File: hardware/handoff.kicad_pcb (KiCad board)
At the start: 2 copper layers, 40 x 62 mm, 55 parts, among them J1 BAT XH-2, J2 PAD JST-XH 2p, J3 LED JST-XH 4p / 5mm RGB, J5 CHG XH-2, J6 MOT 1x02 2.54, Q1 AO3400A, SW1 SS-12F23G5, SW2 TACT 6x6, U1 Raspberry Pi Pico 2 W, U2 MCP6292-E/MS

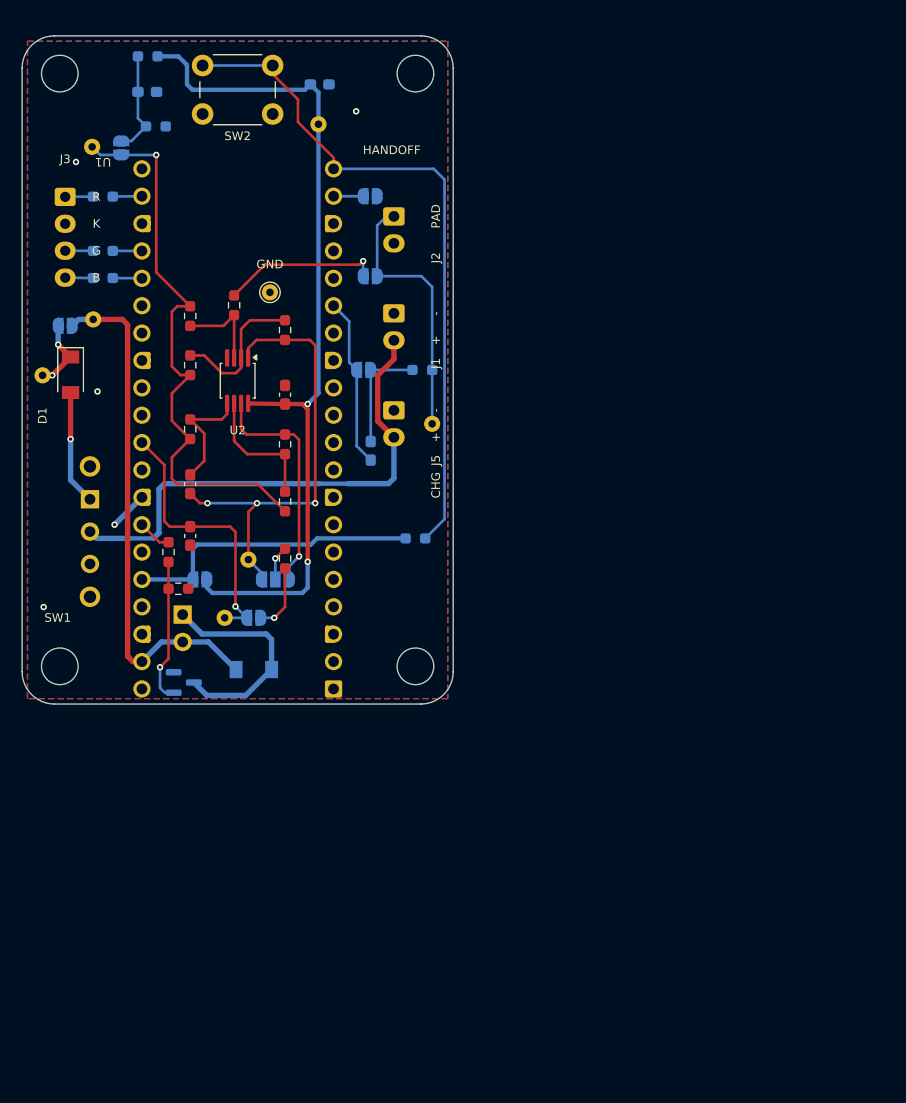
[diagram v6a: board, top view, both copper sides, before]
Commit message: Put the board on the sheet, with fab notes beside it and a title block
The board sat on the page origin, over the sheet border, with a one-line
fab note written across the copper. It now sits at PAGE (40, 35) on the A4
sheet: vec() adds the offset going into pcbnew and at() takes it off coming
out, so every coordinate in gen_pcb.py stays in the floor plan's frame. The
zone outlines appended raw mm() values instead of vec() and are fixed. The
aux and grid origins are the board corner and the fab pack is plotted from
it, so Gerber and drill coordinates are unchanged by the move.

The fab note is a numbered FABRICATION NOTES block on Cmts.User to the
right of the board, and the title block is filled from a SHEET constant
shared with gen_schematic.py so the board and the sheet cannot disagree.

Moving the board exposed a real bug: a fresh BOARD() has no connectivity
until BuildConnectivity() is called, and ZONE_FILLER's island test read
that uninitialised state - the bottom pour's little-finger-wall strip was
kept or dropped, or the whole pour came out empty, depending on where the
board sat. Connectivity is now built before the fill.

Also carries the routing tidy that was in the working tree: AGND's tie out
of pin 33 straight west; TP7 east of D1 on the cathode row with no via;
BTN leaving pin 20 at 45 straight out of the pad; R15 under the Pico on
the +3V3 branch's own row. DRC 0 errors, parity 0, unrouted 0, shorts 0,
19 vias, fab pack 17 files.

Co-Authored-By: Claude Opus 5 <noreply@anthropic.com>
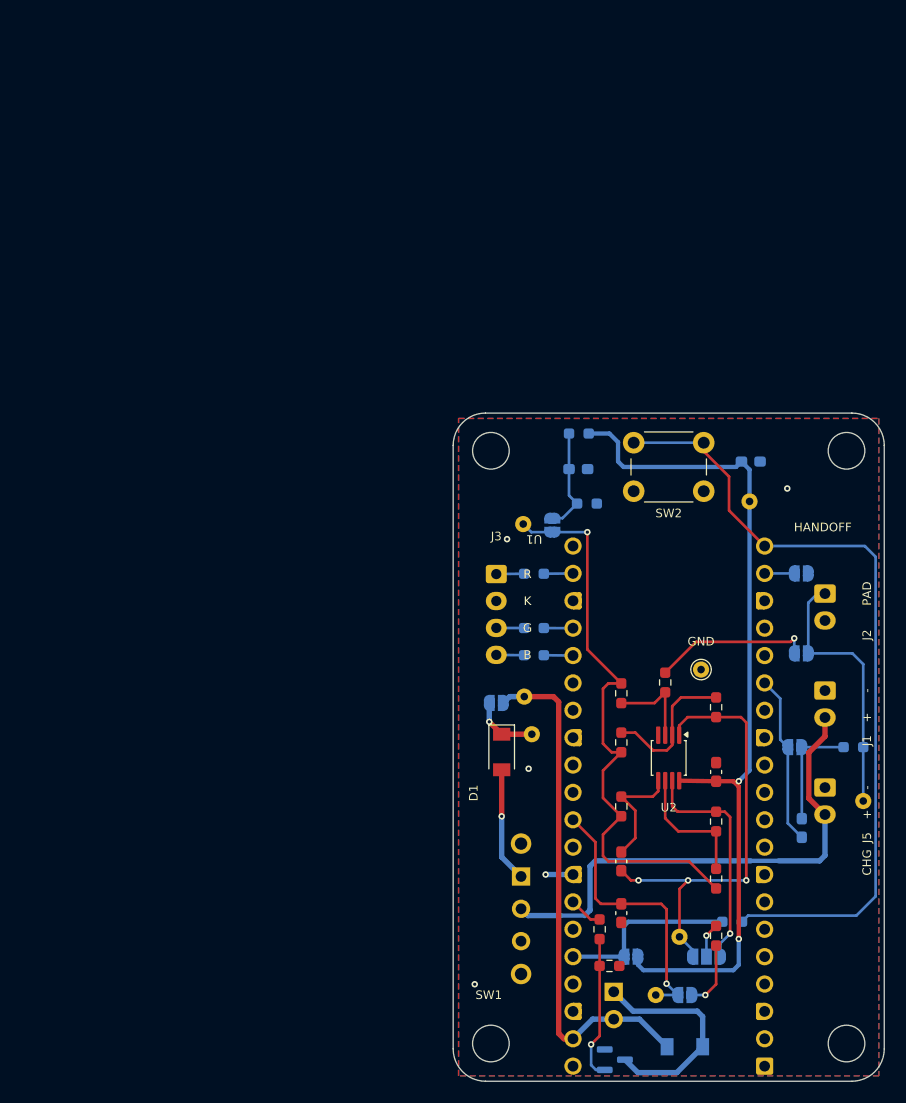
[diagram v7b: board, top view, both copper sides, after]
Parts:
- moved TP7 56.3 mm to (47.3, 64.8)
- moved JP7 53.2 mm to (72.3, 57.3)
- moved JP8 53.2 mm to (72.3, 49.9)
- moved TP8 53.2 mm to (67.5, 43.2)
- moved C2 53.2 mm to (55.6, 81.4)
- moved R7 53.2 mm to (64.4, 72.9)
- moved C3 53.2 mm to (64.4, 68.3)
- moved C4 53.2 mm to (51.6, 40.2)
- moved C5 53.2 mm to (67.6, 39.5)
- moved D1 53.2 mm to (44.5, 66.5)
- moved D3 53.2 mm to (61.5, 93.8)
- moved H1 53.2 mm to (43.5, 38.5)
- moved H2 53.2 mm to (76.5, 38.5)
- moved H3 53.2 mm to (43.5, 93.5)
- moved H4 53.2 mm to (76.5, 93.5)
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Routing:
- net +3V3: track 27.7 -> 16.9 mm
- net /BTN: track 63.2 -> 74.0 mm
- net GND: track 3.59 -> 2.54 mm
- net /D1_K: track 6.68 -> 6.18 mm, vias 2 -> 1
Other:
- board text added: "FABRICATION NOTES 1. Board: 40 x 62 mm, 2 layer, 1.6 mm FR-4, 1 oz Cu, 3.0 mm corner radius. Outline on Edge.Cuts. 2. Finish: HASL lead-free. Green solder mask, white silkscreen. 3. Min track / space: 0.25 / 0.20 mm as designed; 0.15 mm is the fab floor. Min solder-mask dam 0.10 mm. 4. Drills: 0.3, 0.7, 0.95, 1.0, 1.1, 1.15 mm PTH; 3.4 mm NPTH. Tool list in build/drills.md. 5. H1-H4: 3.4 mm unpla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"
- board text removed: "HANDOFF rev A - 2 layer, 40 x 62 mm, 1.6 mm FR-4, 1 oz Cu, HASL lead-free, green mask, white silk. Min track/space 0.25/0.2 (design), 0.15 (fab floor). Min solder-mask dam 0.1. Drills 0.3 / 0.7 / 0.95 / 1.0 / 1.1 / 1.15 PTH and 3.4 NPTH - see build/drills.md. H1-H4 3.4 mm unplated, each inside a 6 mm enclosure boss."

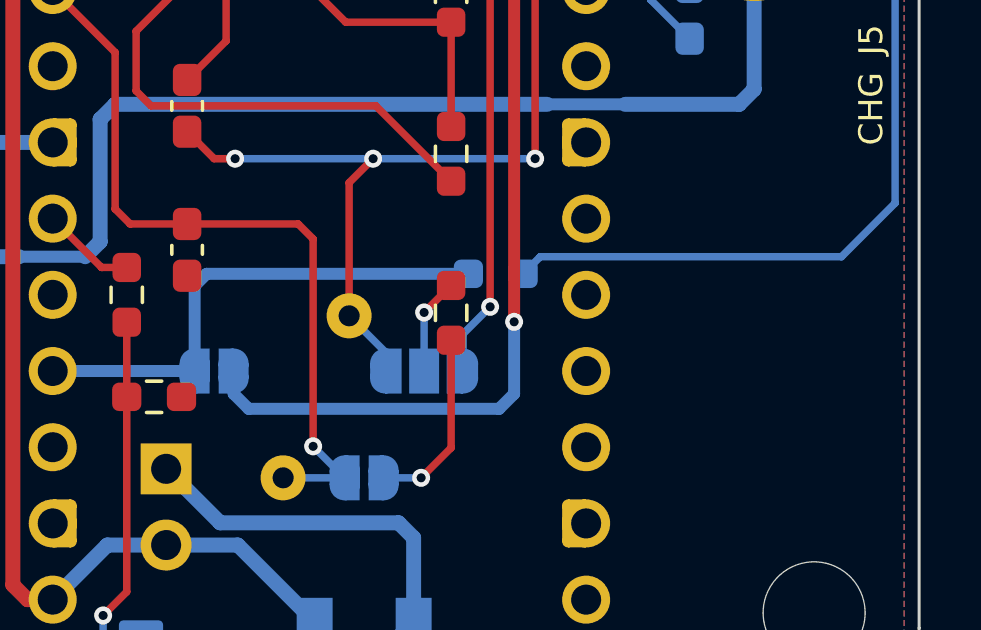
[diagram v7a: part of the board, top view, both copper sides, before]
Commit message: Move R15 west so its +3V3 pad sits directly above JP4's
R15 was at x 25.9 with the +3V3 branch running 10 mm along y 47.2 to
reach it. It now sits at (16.7625, 47.2), which puts pad 1 on x 15.85, the
same vertical as JP4's +3V3 pad: the branch is one straight leg north out
of the jumper pad, 3.2 mm, with no bends. BTN leaves pad 2, steps onto
y 46.63 with the same 45 as before and runs that row east to pin 6/7's
gap. DRC 0 errors, parity 0, unrouted 0, shorts 0; 19 vias, fab pack 17.

Also ignores hardware/.history/, an editor local-history folder.

Co-Authored-By: Claude Opus 5 <noreply@anthropic.com>
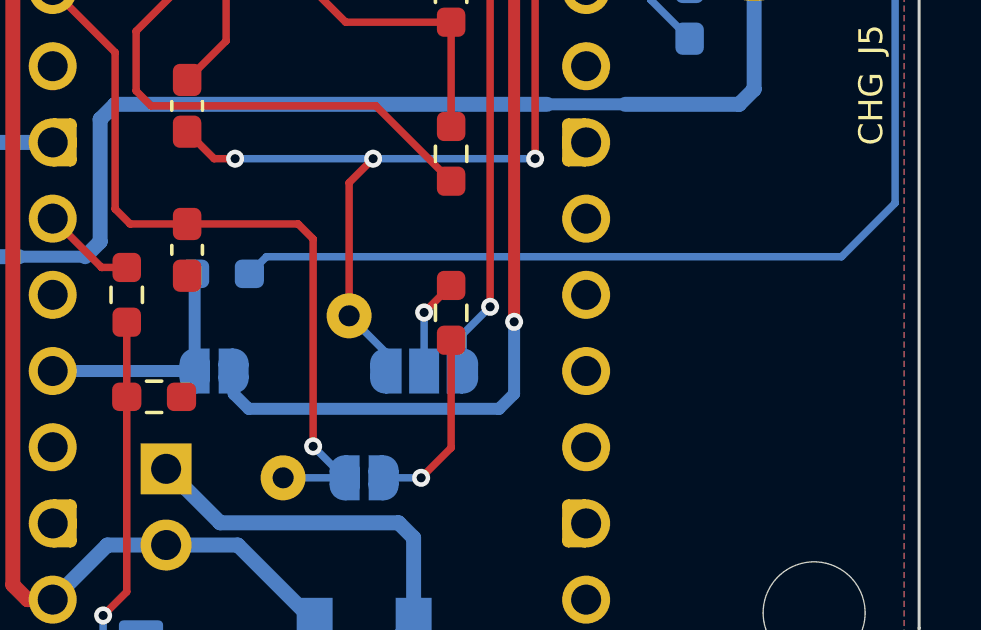
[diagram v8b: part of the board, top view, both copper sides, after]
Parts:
- moved R15 9.12 mm to (56.8, 82.2)
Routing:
- net /BTN: track 74.0 -> 83.1 mm
- net +3V3: track 16.9 -> 7.97 mm
